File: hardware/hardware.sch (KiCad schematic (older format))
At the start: 18 parts, among them J1 Conn_01x04_Male, J2 Teensy3.2, J3 DIN-5_180degree, J4 TeensyAudioShield3.2, J5 DIN-5_180degree, SW1 SW_Push, SW2 SW_Push, U1 6N139

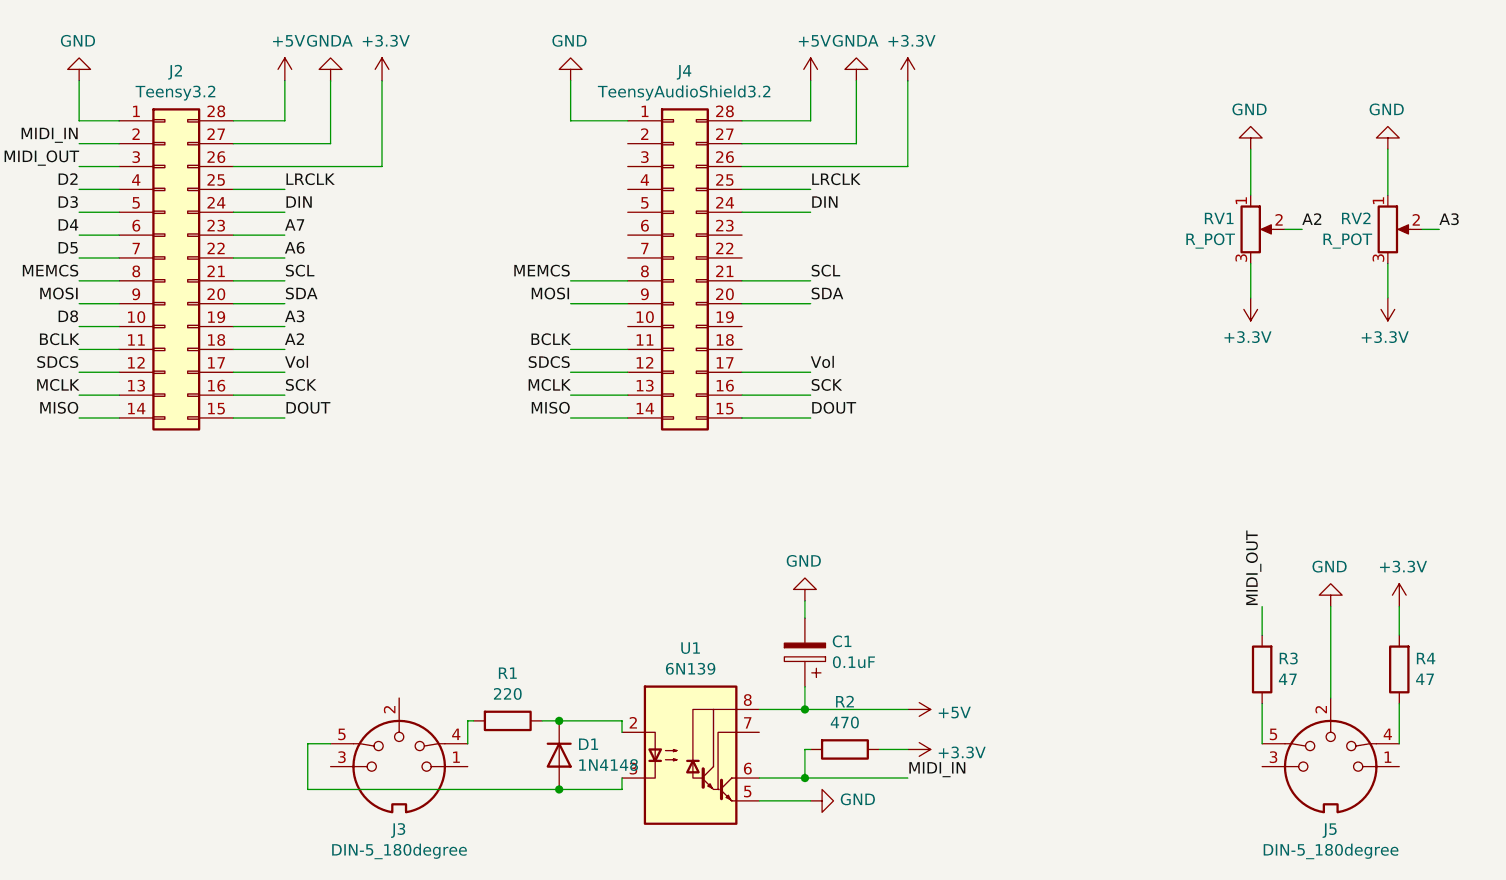
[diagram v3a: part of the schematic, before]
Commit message: Schematic changes
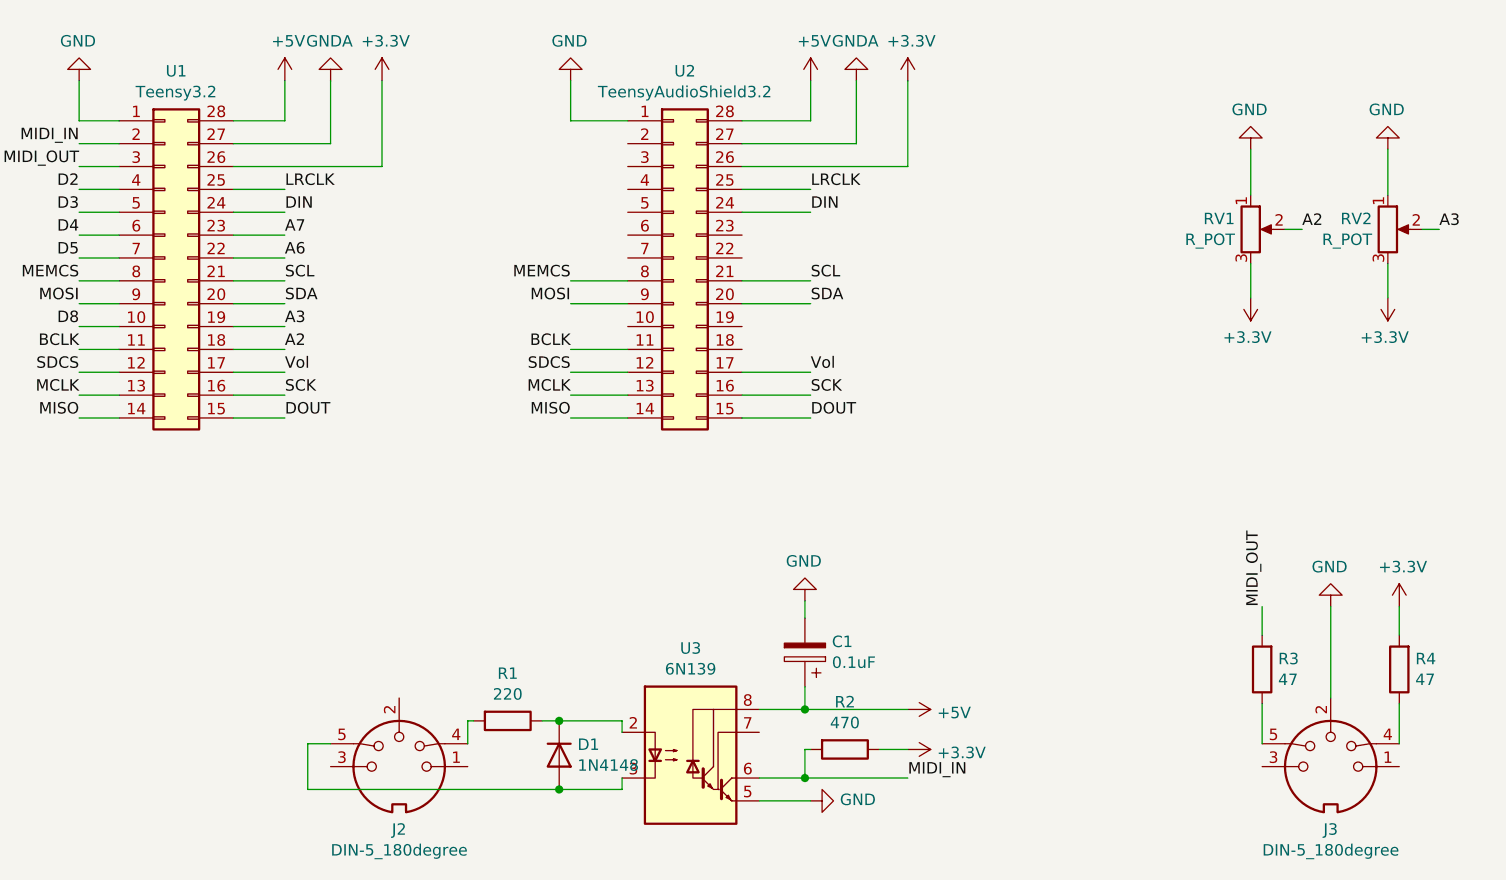
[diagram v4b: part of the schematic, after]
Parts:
- renumbered J3 to J2, J5 to J3, J2 to U1, J4 to U2, U1 to U3
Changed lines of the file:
@@
 $EndDescr
 $Comp
-L Connector:DIN-5_180degree J5
+L Connector:DIN-5_180degree J3
 U 1 1 5FB453D9
 P 8100 4250
-F 0 "J5" H 8100 3975 50  0000 C CNN
+F 0 "J3" H 8100 3975 50  0000 C CNN
 F 1 "DIN-5_180degree" H 8100 3884 50  0000 C CNN
 F 2 "hardware:SDS-50J" H 8100 4250 50  0001 C CNN
@@
 $EndComp
 $Comp
-L Connector:DIN-5_180degree J3
+L Connector:DIN-5_180degree J2
 U 1 1 5FB4610C
 P 4025 4250
-F 0 "J3" H 4025 3975 50  0000 C CNN
+F 0 "J2" H 4025 3975 50  0000 C CNN
 F 1 "DIN-5_180degree" H 4025 3884 50  0000 C CNN
 F 2 "hardware:SDS-50J" H 4025 4250 50  0001 C CNN
@@
 $EndComp
 $Comp
-L Isolator:6N139 U1
+L Isolator:6N139 U3
 U 1 1 5FB479F7
 P 5300 4200
-F 0 "U1" H 5300 4667 50  0000 C CNN
+F 0 "U3" H 5300 4667 50  0000 C CNN
 F 1 "6N139" H 5300 4576 50  0000 C CNN
 F 2 "Package_DIP:DIP-8_W7.62mm_Socket_LongPads" H 5590 3900 50  0001 C CNN
@@
 $EndComp
 $Comp
-L hardware:Teensy3.2 J2
+L hardware:Teensy3.2 U1
 U 1 1 5FB4EEE5
 P 3000 2025
-F 0 "J2" H 3050 2842 50  0000 C CNN
+F 0 "U1" H 3050 2842 50  0000 C CNN
 F 1 "Teensy3.2" H 3050 2751 50  0000 C CNN
 F 2 "hardware:Teensy3.2" H 3000 2025 50  0001 C CNN
@@
 $EndComp
 $Comp
-L hardware:TeensyAudioShield3.2 J4
+L hardware:TeensyAudioShield3.2 U2
 U 1 1 5FB51D0C
 P 5225 2025
-F 0 "J4" H 5275 2842 50  0000 C CNN
+F 0 "U2" H 5275 2842 50  0000 C CNN
 F 1 "TeensyAudioShield3.2" H 5275 2751 50  0000 C CNN
 F 2 "hardware:TeensyArduinoShield3.2" H 5225 2025 50  0001 C CNN

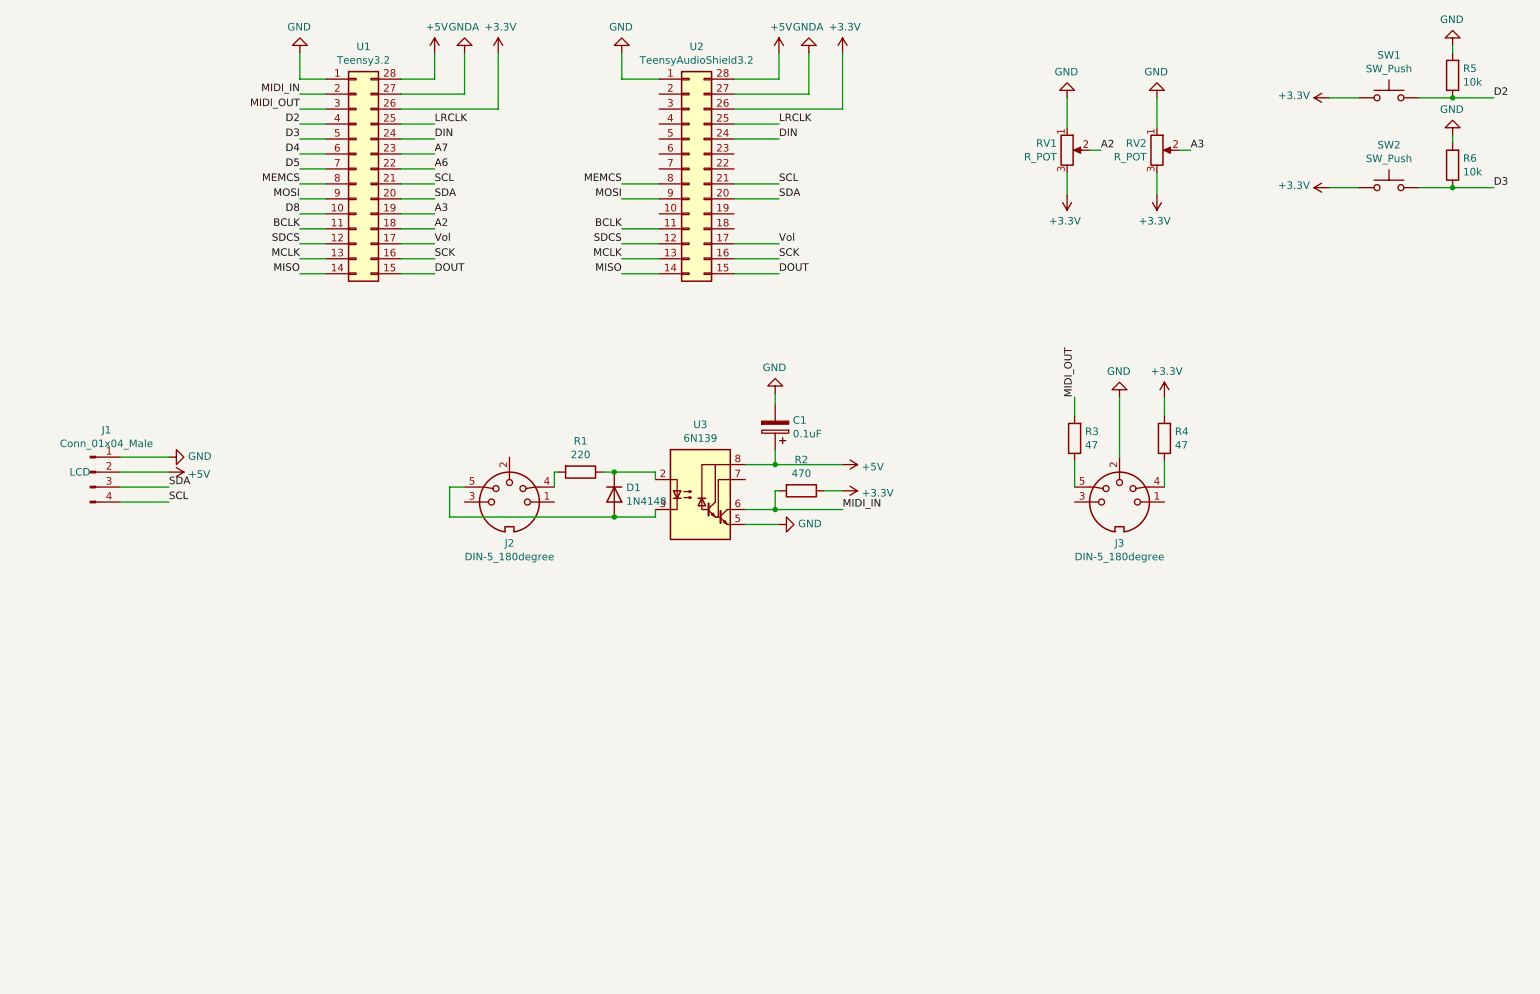
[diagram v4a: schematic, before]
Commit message: Add multiplexer and update pcb
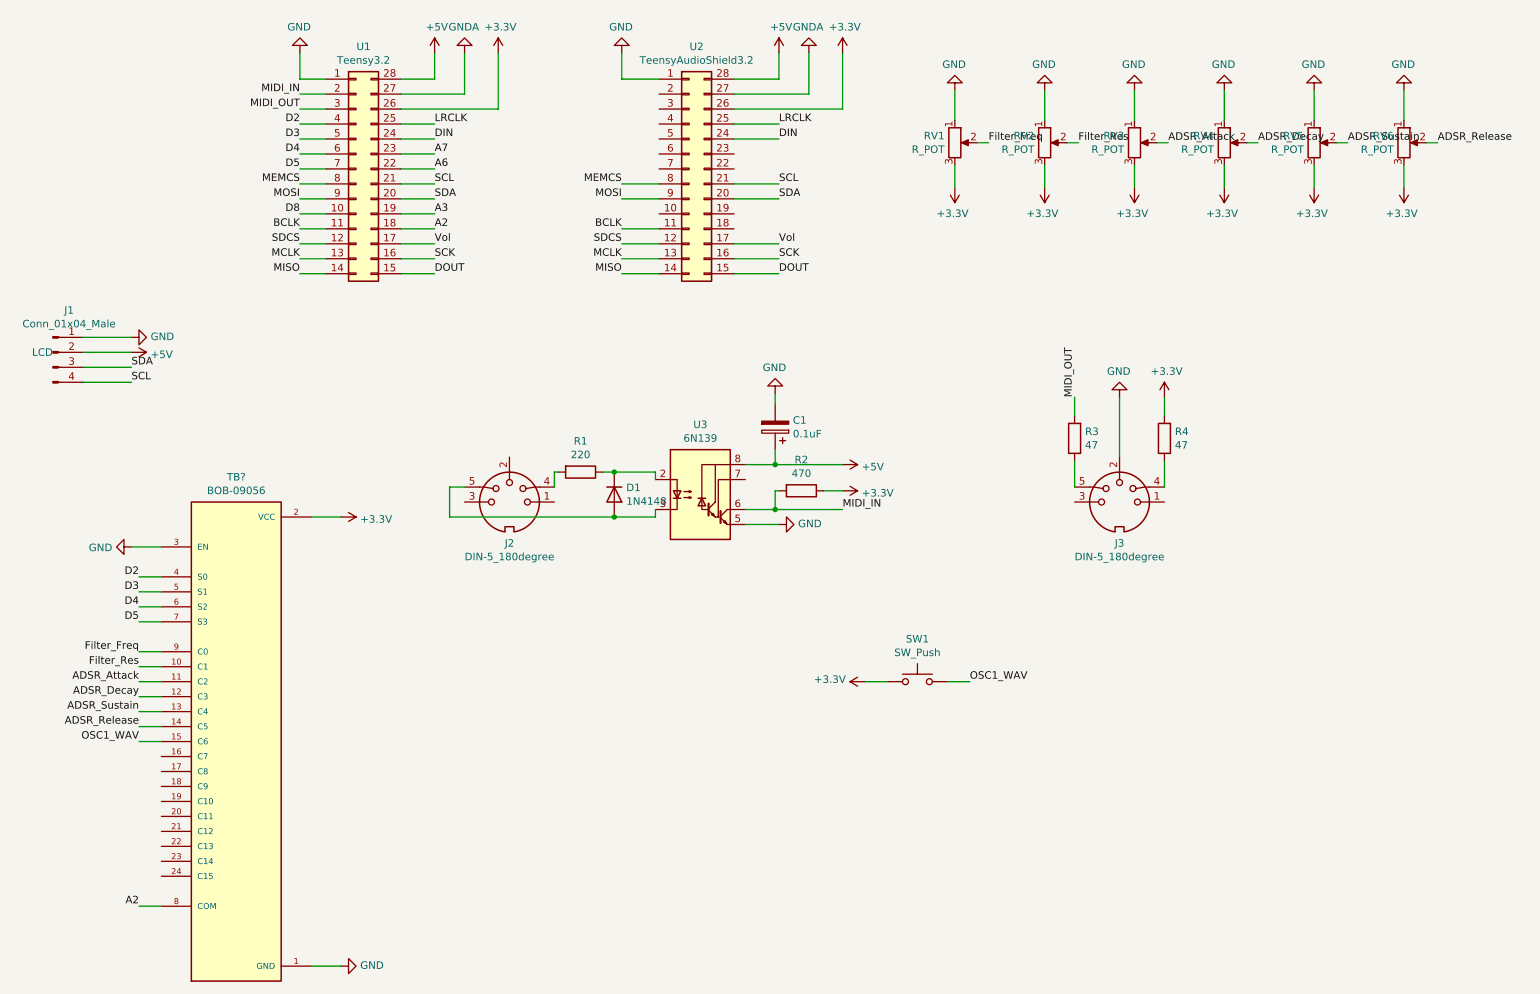
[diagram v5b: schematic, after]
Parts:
- removed R5, R6: 10k, Resistor_THT:R_Axial_DIN0207_L6.3mm_D2.5mm_P10.16mm_Horizontal, symbol Device:R
- removed SW2: SW_Push, Button_Switch_THT:SW_PUSH-12mm, symbol Switch:SW_Push
- added RV3, RV4, RV5, RV6: R_POT, Potentiometer_THT:Potentiometer_Alpha_RD901F-40-00D_Single_Vertical_CircularHoles, symbol Device:R_POT
- added TB?: BOB-09056, XDCR_BOB-09056, symbol BOB-09056:BOB-09056
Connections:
- net +3V3: now also RV3.3, RV4.3, RV5.3, RV6.3, TB?.2 (VCC)
- net A2: now also TB?.8 (COM); no longer RV1.2
- net A3: no longer RV2.2
- net D2: now also TB?.4 (S0); no longer SW1.2
- net D3: now also TB?.5 (S1)
- net D4: now also TB?.6 (S2)
- net D5: now also TB?.7 (S3)
- net GND: now also RV3.1, RV4.1, RV5.1, RV6.1, TB?.1 (GND), TB?.3 (EN)
- new net ADSR_Attack: RV3.2, TB?.11 (C2)
- new net ADSR_Decay: RV4.2, TB?.12 (C3)
- new net ADSR_Release: RV6.2, TB?.14 (C5)
- new net ADSR_Sustain: RV5.2, TB?.13 (C4)
- new net Filter_Freq: RV1.2, TB?.9 (C0)
- new net Filter_Res: RV2.2, TB?.10 (C1)
- new net OSC1_WAV: SW1.2, TB?.15 (C6)
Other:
- moved on the sheet: J1, RV1, RV2

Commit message: Layout pcb
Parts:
- gave numbers to parts that had none: 1
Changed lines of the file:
@@
 	6950 5450 7100 5450
 $Comp
-L BOB-09056:BOB-09056 TB?
+L BOB-09056:BOB-09056 TB1
 U 1 1 5FC108A3
 P 2200 5850
-F 0 "TB?" H 2200 7617 50  0000 C CNN
+F 0 "TB1" H 2200 7617 50  0000 C CNN
 F 1 "BOB-09056" H 2200 7526 50  0000 C CNN
 F 2 "XDCR_BOB-09056" H 2200 5850 50  0001 L BNN
@@
 $EndComp
 $Comp
-L power:GND #PWR?
+L power:GND #PWR0129
 U 1 1 5FC17AFF
 P 2900 7350
-F 0 "#PWR?" H 2900 7100 50  0001 C CNN
+F 0 "#PWR0129" H 2900 7100 50  0001 C CNN
 F 1 "GND" V 2905 7222 50  0000 R CNN
 F 2 "" H 2900 7350 50  0001 C CNN
@@
 $EndComp
 $Comp
-L power:GND #PWR?
+L power:GND #PWR0130
 U 1 1 5FC184AB
 P 1500 4550
-F 0 "#PWR?" H 1500 4300 50  0001 C CNN
+F 0 "#PWR0130" H 1500 4300 50  0001 C CNN
 F 1 "GND" V 1505 4422 50  0000 R CNN
 F 2 "" H 1500 4550 50  0001 C CNN
@@
 	2900 7350 2700 7350
 $Comp
-L power:+3.3V #PWR?
+L power:+3.3V #PWR0132
 U 1 1 5FC260F2
 P 2900 4350
-F 0 "#PWR?" H 2900 4200 50  0001 C CNN
+F 0 "#PWR0132" H 2900 4200 50  0001 C CNN
 F 1 "+3.3V" V 2915 4478 50  0000 L CNN
 F 2 "" H 2900 4350 50  0001 C CNN
